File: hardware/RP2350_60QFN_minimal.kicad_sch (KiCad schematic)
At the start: 43 parts, among them J1 USB_B_Micro, J2 Conn_02x18_Odd_Even, J3 Conn_02x18_Odd_Even, J4 SM03B-SRSS-TB, SW1 SW_Push, SW2 SW_Push, U1 RP2350_60QFN, U2 NCP1117-3.3_SOT223, U3 W25Q128JVS, Y1 ABM8-272-T3

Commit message: feat(hardware): Add 8MB PSRAM Flash
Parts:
- removed J2, J3: Conn_02x18_Odd_Even, Connector_PinHeader_2.54mm:PinHeader_2x18_P2.54mm_Vertical, symbol Connector_Generic:Conn_02x18_Odd_Even
- removed R1, R9: DNF, Resistor_SMD:R_0402_1005Metric, symbol Device:R
- removed R10: 0, Resistor_SMD:R_0402_1005Metric, symbol Device:R
- added C20: 100n, symbol Device:C
- added J5: 4677, SOIC127P600X175-8N, symbol 4677:4677
- added R3: 100k, symbol Device:R
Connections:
- net QSPI_SS is gone; now on net ~{FLASH_CS}: R6.1, U1.60 (QSPI_SS)
- net +3V3: now also C20.1, J5.8 (VCC), R3.1
- net GND: now also C20.2, J5.4 (VSS)
- net QSPI_SCLK: now also J5.6 (SCLK)
- net QSPI_SD0: now also J5.5 (SI/SIO[0])
- net QSPI_SD1: now also J5.2 (SO/SIO[1])
- net QSPI_SD2: now also J5.3 (SIO[2])
- net QSPI_SD3: now also J5.7 (SIO[3])
- net FLASH_SS renamed ~{FLASH_CS}
- net GPIO0: no longer names the net of U1.2 (GPIO0)
- net GPIO1: no longer names the net of U1.3 (GPIO1)
- net GPIO10: no longer names the net of U1.14 (GPIO10)
- net GPIO11: no longer names the net of U1.15 (GPIO11)
- net GPIO12: no longer names the net of U1.16 (GPIO12)
- net GPIO13: no longer names the net of U1.17 (GPIO13)
- net GPIO14: no longer names the net of U1.18 (GPIO14)
- net GPIO15: no longer names the net of U1.19 (GPIO15)
- net GPIO16: no longer names the net of U1.27 (GPIO16)
- net GPIO17: no longer names the net of U1.28 (GPIO17)
- net GPIO18: no longer names the net of U1.29 (GPIO18)
- net GPIO19: no longer names the net of U1.31 (GPIO19)
- net GPIO2: no longer names the net of U1.4 (GPIO2)
- net GPIO20: no longer names the net of U1.32 (GPIO20)
- net GPIO21: no longer names the net of U1.33 (GPIO21)
- net GPIO22: no longer names the net of U1.34 (GPIO22)
- net GPIO23: no longer names the net of U1.35 (GPIO23)
- net GPIO24: no longer names the net of U1.36 (GPIO24)
- net GPIO25: no longer names the net of U1.37 (GPIO25)
- net GPIO3: no longer names the net of U1.5 (GPIO3)
- net GPIO4: no longer names the net of U1.7 (GPIO4)
- net GPIO5: no longer names the net of U1.8 (GPIO5)
- net GPIO6: no longer names the net of U1.9 (GPIO6)
- net GPIO7: no longer names the net of U1.10 (GPIO7)
- net GPIO8 renamed ~{PSRAM_CS}
- net ~{PSRAM_CS}: now also J5.1 (CE#), R3.2
- net GPIO9: no longer names the net of U1.13 (GPIO9)
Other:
- note added: "PSRAM"
- note removed: "IOs"
- moved on the sheet: C1, C10, C11, C12, C13, C14, C15, C16, C17, C18, C19, C2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

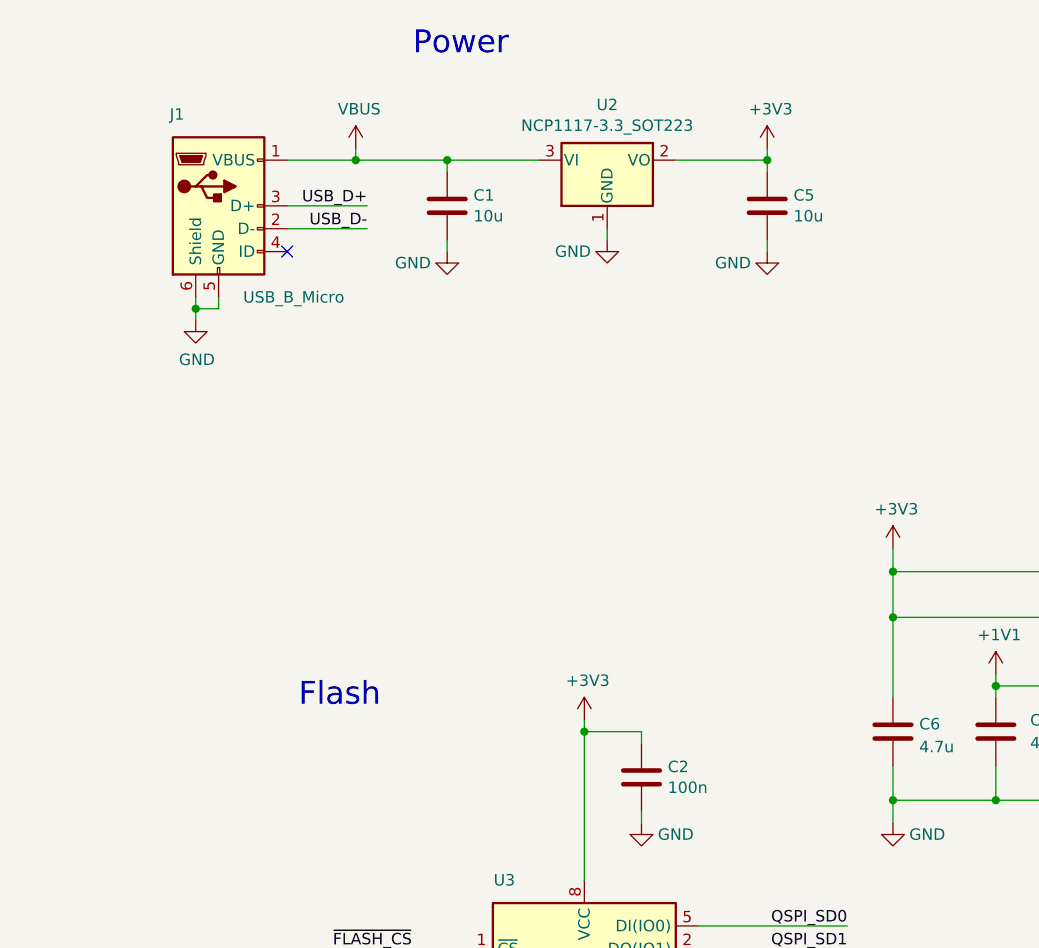
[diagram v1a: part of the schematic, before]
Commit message: feat(hardware): Swap Micro USB with USB C
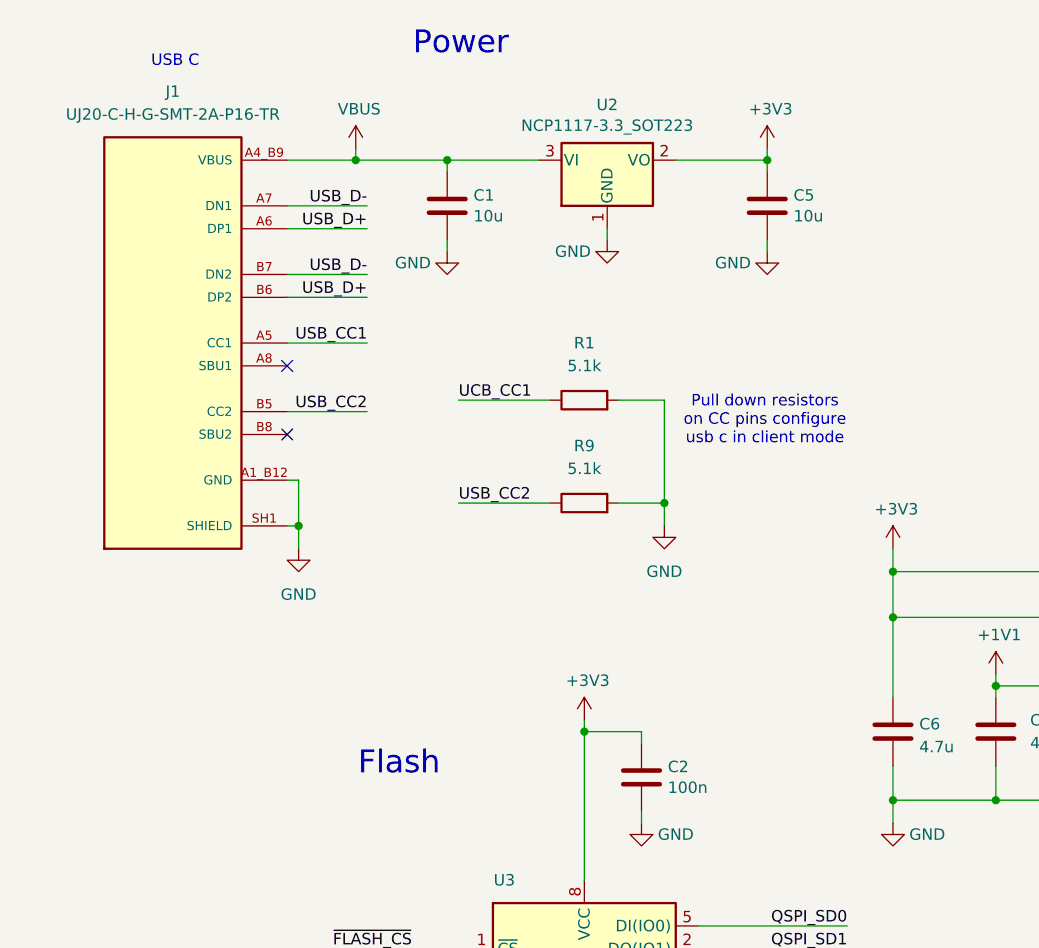
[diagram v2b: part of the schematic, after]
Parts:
- removed J1: USB_B_Micro, Connector_USB:USB_Micro-B_Amphenol_10103594-0001LF_Horizontal, symbol Connector:USB_B_Micro
- added J1: UJ20-C-H-G-SMT-2A-P16-TR, UJ20-C-H-G-SMT-1-P16-TR:SAMESKY_UJ20-C-H-G-SMT-1-P16-TR, symbol UJ20-C-H-G-SMT-1-P16-TR:UJ20-C-H-G-SMT-1-P16-TR
- added R1, R9: 5.1k, symbol Device:R
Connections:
- net GND: now also J1.A1_B12 (GND), J1.B1_A12 (GND), J1.SH1 (SHIELD), J1.SH2 (SHIELD), J1.SH3 (SHIELD), J1.SH4 (SHIELD), R1.2, R9.2
- net USB_D+: now also J1.A6 (DP1), J1.B6 (DP2)
- net USB_D-: now also J1.A7 (DN1), J1.B7 (DN2)
- net VBUS: now also J1.A4_B9 (VBUS), J1.B4_A9 (VBUS)
- new net UCB_CC1: R1.1
- new net USB_CC1: J1.A5 (CC1)
- new net USB_CC2: J1.B5 (CC2), R9.1
- no-connect marks 1 -> 2
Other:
- note added: "Pull down resistors on CC pins configure usb c in client mode"
- note added: "USB C"

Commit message: added digital psu
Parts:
- removed C5: 10u, Capacitor_SMD:C_0805_2012Metric, symbol Device:C
- removed U2: NCP1117-3.3_SOT223, Package_TO_SOT_SMD:SOT-223-3_TabPin2, symbol Regulator_Linear:NCP1117-3.3_SOT223
- added C21: 2.2uF, symbol Device:C
- added U2: MIC5205-3.3YM5, Package_TO_SOT_SMD:SOT-23-5, symbol Regulator_Linear:MIC5205-3.3YM5
- C1: value 10u -> 470pF; footprint Capacitor_SMD:C_0805_2012Metric -> (none)
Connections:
- net GND: now also C21.2, U2.2 (GND)
- net VBUS: now also U2.1 (IN), U2.3 (EN); no longer C1.1
- new net: C1.1, U2.4 (BP)
- new net: C21.1, U2.5 (OUT)
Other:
- added sheet PSU (PSU.kicad_sch)
- note added: "Analog will be done tomorrow"
- note added: "Power for Digital Components. Input voltage range from 2.5V to 16V (from USB C) with a fixed output of 3.3V."
- moved on the sheet: J1, R1, R9

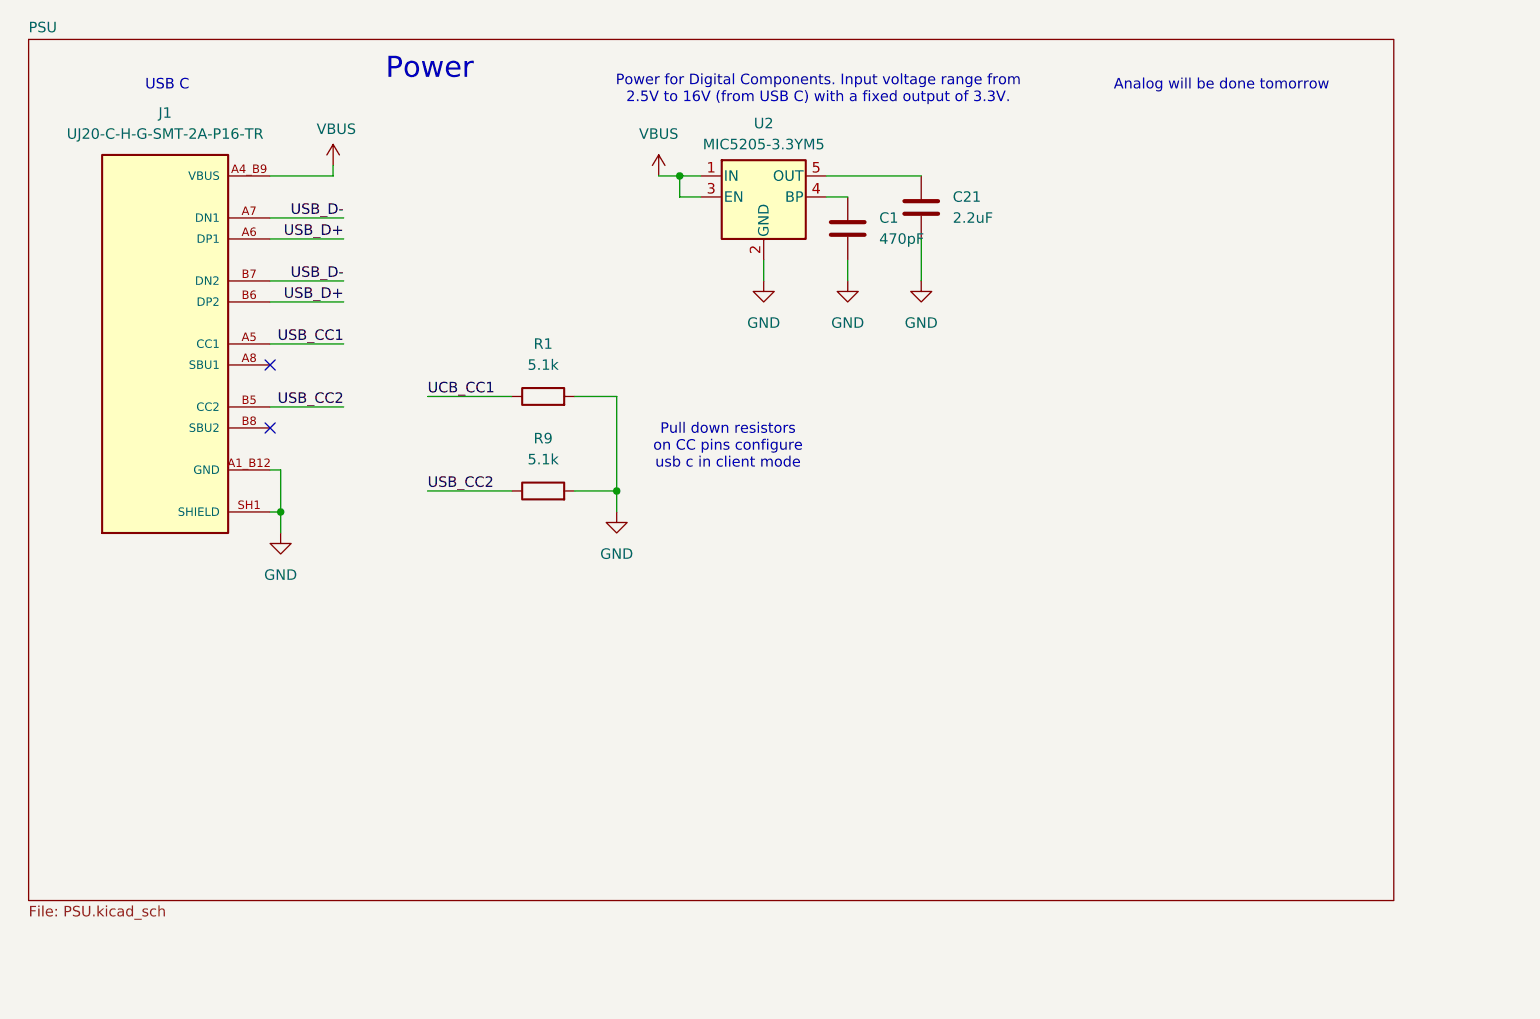
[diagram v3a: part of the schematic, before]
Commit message: added analog psu, needs review
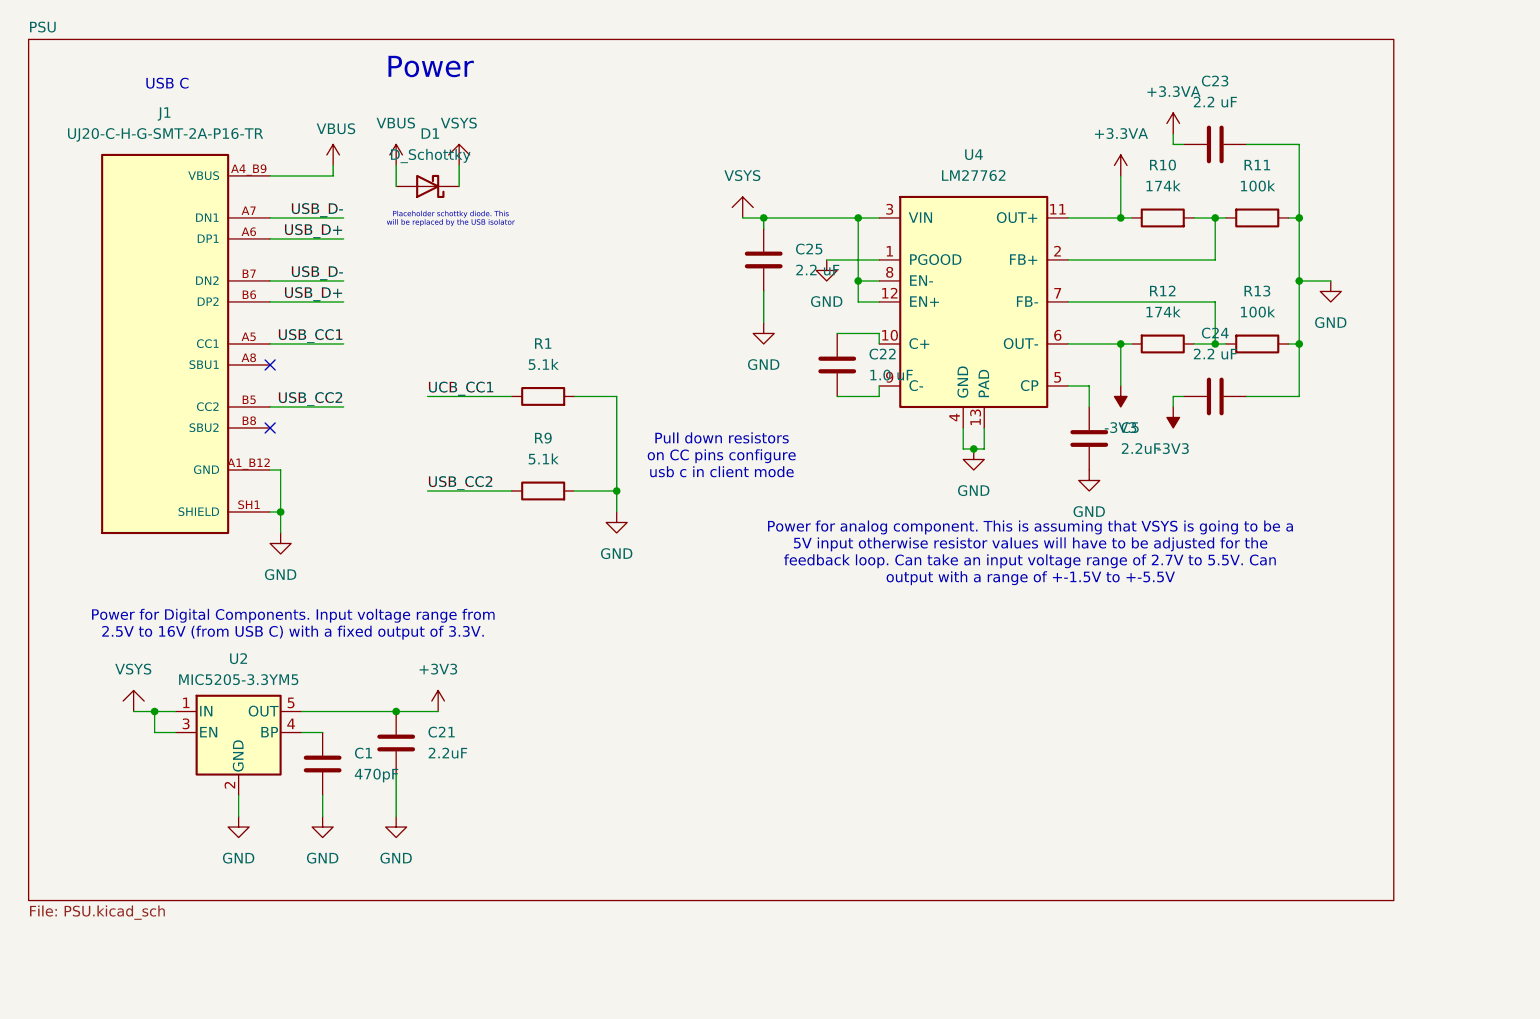
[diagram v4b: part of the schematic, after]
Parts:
- added C22: 1.0 uF, symbol Device:C
- added C23, C24, C25: 2.2 uF, symbol Device:C
- added C5: 2.2uF, symbol Device:C
- added D1: D_Schottky, symbol Device:D_Schottky
- added R10, R12: 174k, symbol Device:R
- added R11, R13: 100k, symbol Device:R
- added U4: LM27762, Package_SON:WSON-12-1EP_3x2mm_P0.5mm_EP1x2.65_ThermalVias, symbol Regulator_SwitchedCapacitor:LM27762
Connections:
- net +3V3: now also C21.1, U2.5 (OUT)
- net GND: now also C23.2, C24.2, C25.2, C5.2, R11.1, R13.1, U4.1 (PGOOD), U4.13 (PAD), U4.4 (GND)
- net VBUS: now also D1.2 (A); no longer U2.1 (IN), U2.3 (EN)
- new net: R12.1, R13.2, U4.7 (FB-)
- new net: C5.1, U4.5 (CP)
- new net: C22.1, U4.10 (C+)
- new net: C22.2, U4.9 (C-)
- new net: R10.2, R11.2, U4.2 (FB+)
- new net +3.3VA: C23.1, R10.1, U4.11 (OUT+)
- new net -3V3: C24.1, R12.2, U4.6 (OUT-)
- new net VSYS: C25.1, D1.1 (K), U2.1 (IN), U2.3 (EN), U4.12 (EN+), U4.3 (VIN), U4.8 (EN-)
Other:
- note added: "Placeholder schottky diode. This will be replaced by the USB isolator"
- note added: "Power for analog component. This is assuming that VSYS is going to be a 5V input otherwise resistor values will have to be adjusted for the feedback loop. Can take an input voltage range of 2.7V to 5.5V. Can output with a range of +-1.5V to +-5.5V"
- note removed: "Analog will be done tomorrow"
- moved on the sheet: C1, C21, U2

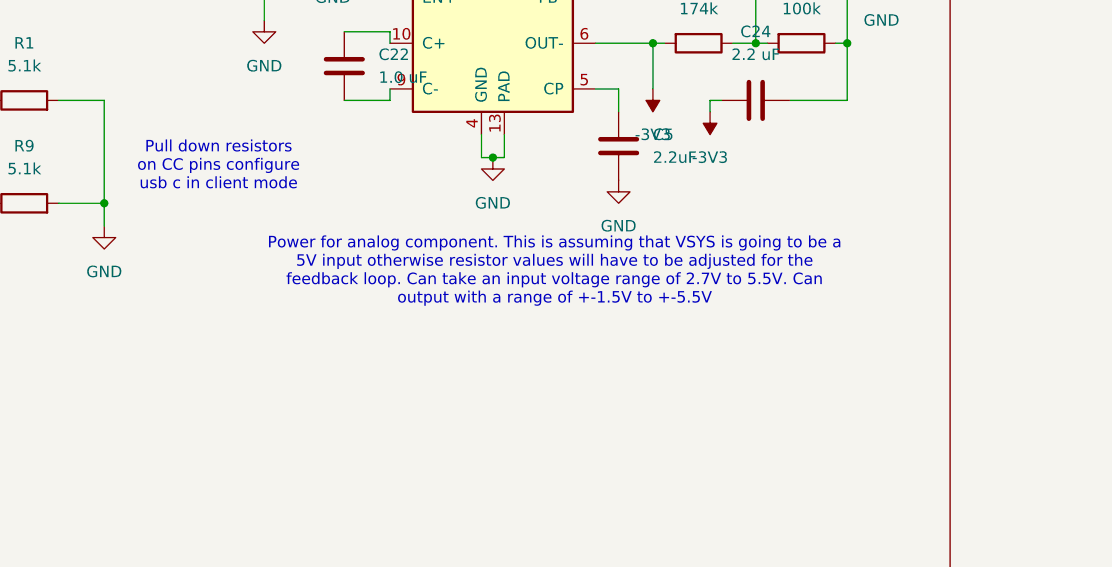
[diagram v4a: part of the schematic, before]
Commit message: added links and prices
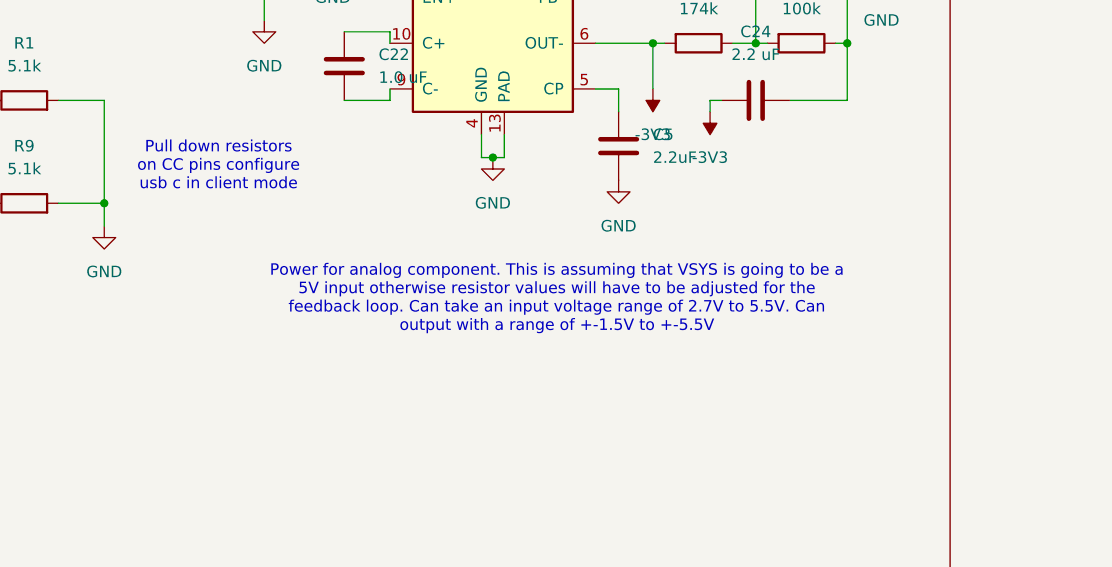
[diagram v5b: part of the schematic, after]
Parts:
- U4: Price (none) -> $0.76; Purchase Link (none) -> https://www.ti.com/product/LM27762
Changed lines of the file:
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@@
 	(text "Power for analog component. This is assuming that VSYS is going to be a \n5V input otherwise resistor values will have to be adjusted for the \nfeedback loop. Can take an input voltage range of 2.7V to 5.5V. Can \noutput with a range of +-1.5V to +-5.5V"
 		(exclude_from_sim no)
-		(at 136.398 78.74 0)
+		(at 136.652 81.788 0)
 		(effects
 			(font
@@
 			(at 128.27 43.18 0)
 			(effects
+				(font
+					(size 1.27 1.27)
+				)
+				(hide yes)
+			)
+		)
+		(property "Price" "$0.76"
+			(at 128.27 43.18 0)
+			(effects
+				(font
+					(size 1.27 1.27)
+				)
+				(hide yes)
+			)
+		)
+		(property "Purchase Link" "https://www.ti.com/product/LM27762"
+			(at 128.27 43.18 0)
+			(effects
